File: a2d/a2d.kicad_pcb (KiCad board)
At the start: 4 copper layers, 70 x 65.8 mm, 67 parts, among them CN1 BM04B-SRSS-TB(LF)(SN), U1 B3B-XH-A(LF)(SN), U10 B3B-XH-A(LF)(SN), U2 2060-453/998-404, U3 ADM7150ARDZ-5.0, U4 ADS1115IDGSR, U5 2060-453/998-404, U6 B3B-XH-A(LF)(SN), U7 2060-453/998-404, U8 B3B-XH-A(LF)(SN), U9 2060-453/998-404

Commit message: fix large cap
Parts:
- removed C8: 47uF, Capacitor_SMD:C_0603_1608Metric
- C13: value 47uF -> 47uf; footprint Capacitor_SMD:C_0603_1608Metric -> Capacitor_Tantalum_SMD:CP_EIA-7343-43_Kemet-X
- C18, C2, C22, C26, C27, C7: value .1uf -> 100nf
- moved C13 8.30 mm to (33.3, 30.6), turned to 180 degrees
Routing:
- net +5V: track 35.0 -> 41.3 mm
- net /6V: track 20.4 -> 18.8 mm
- net GND: vias 45 -> 48

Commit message: add second i2c connector
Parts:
- added C14: 1uf, Capacitor_SMD:C_0603_1608Metric, F.Cu at (53.8, 74.0)
- added C29: 10uf, Capacitor_SMD:C_0603_1608Metric, F.Cu at (55.4, 74.0)
- added C8: 100nf, Capacitor_SMD:C_0603_1608Metric, F.Cu at (52.2, 74.0)
- added CN2: BM04B-SRSS-TB(LF)(SN), easyeda2kicad:CONN-SMD_BM04B-SRSS-TB, F.Cu at (50.0, 78.0)
- added D6: SP0503BAHT, Package_TO_SOT_SMD:SOT-143, F.Cu at (49.6, 73.8)
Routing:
- net /6V: track 18.8 -> 101.4 mm, vias 0 -> 5
- net /SCL: track 37.2 -> 66.0 mm, vias 2 -> 3
- net /SDA: track 37.6 -> 63.1 mm, vias 2 -> 3
- net GND: track 63.3 -> 66.8 mm, vias 48 -> 55

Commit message: a2d v0.2
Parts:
- added J1: Conn_02x04_Odd_Even, Connector_PinHeader_2.54mm:PinHeader_2x04_P2.54mm_Vertical, F.Cu at (26.9, 53.8)
- added JP1: Jumper_2_Small_Open, Connector_PinHeader_2.54mm:PinHeader_1x02_P2.54mm_Vertical, F.Cu at (60.8, 49.2)
- added JP2: Jumper_2_Small_Open, Connector_PinHeader_2.54mm:PinHeader_1x02_P2.54mm_Vertical, F.Cu at (61.0, 71.8)
- added JP3: Jumper_2_Small_Open, Connector_PinHeader_2.54mm:PinHeader_1x02_P2.54mm_Vertical, F.Cu at (41.2, 56.6)
- added JP4: Jumper_2_Small_Open, Connector_PinHeader_2.54mm:PinHeader_1x02_P2.54mm_Vertical, F.Cu at (42.8, 32.4)
- C1, C16, C18, C2, C20, C22, C24, C26: value 100nf -> 100nF
- C15, C19, C23, C3: value 10uf -> 10uF
- C17, C21, C25, C4: value 1uf -> 1uF
- R2, R4, R6, R8: value 100k -> 5.1M
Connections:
- R2 pad 1: GND -> Net-(JP1-A)
- R4 pad 1: GND -> Net-(JP2-A)
- R6 pad 1: GND -> Net-(JP3-A)
- R8 pad 1: GND -> Net-(JP4-A)
- U4 pad 1: GND -> Net-(J1-Pin_2)
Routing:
- net Net-(J1-Pin_2): track 0.00 -> 23.2 mm
- net /SCL: track 66.0 -> 86.4 mm, vias 3 -> 5
- net /SDA: track 63.1 -> 79.8 mm
- net Net-(JP1-A): track 0.00 -> 10.5 mm
- net Net-(JP2-A): track 0.00 -> 9.75 mm
- net Net-(JP3-A): track 0.00 -> 9.15 mm
- net Net-(JP4-A): track 0.00 -> 8.03 mm
- net /6V: track 101.4 -> 103.9 mm
- net GND: track 66.8 -> 64.9 mm, vias 55 -> 51
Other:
- board text added: "1"
- board text added: "2"
- board text added: "3"
- board text added: "4"
- board text added: "A2D V0.2"
- board text added: "Address:"
- board text removed: "A2D V0.1"

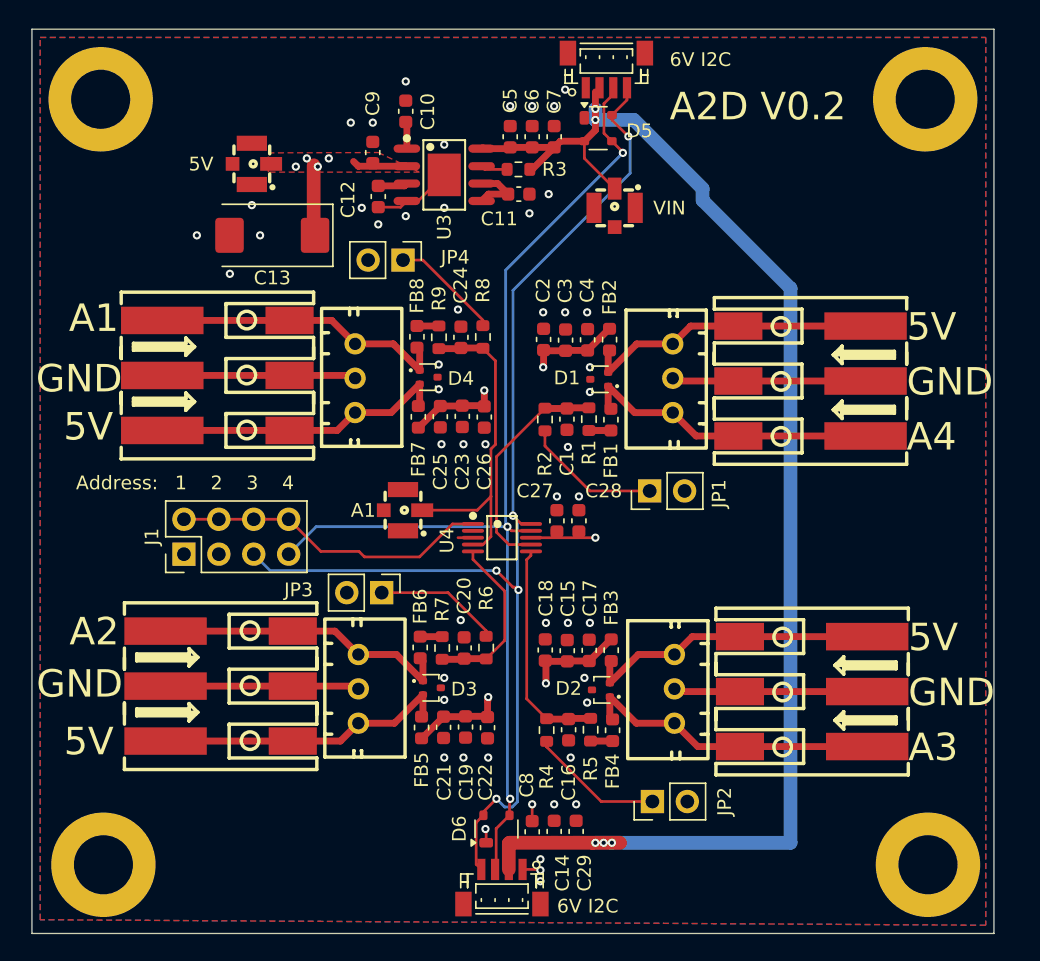
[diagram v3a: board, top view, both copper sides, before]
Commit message: reverse connector orientation for a2d
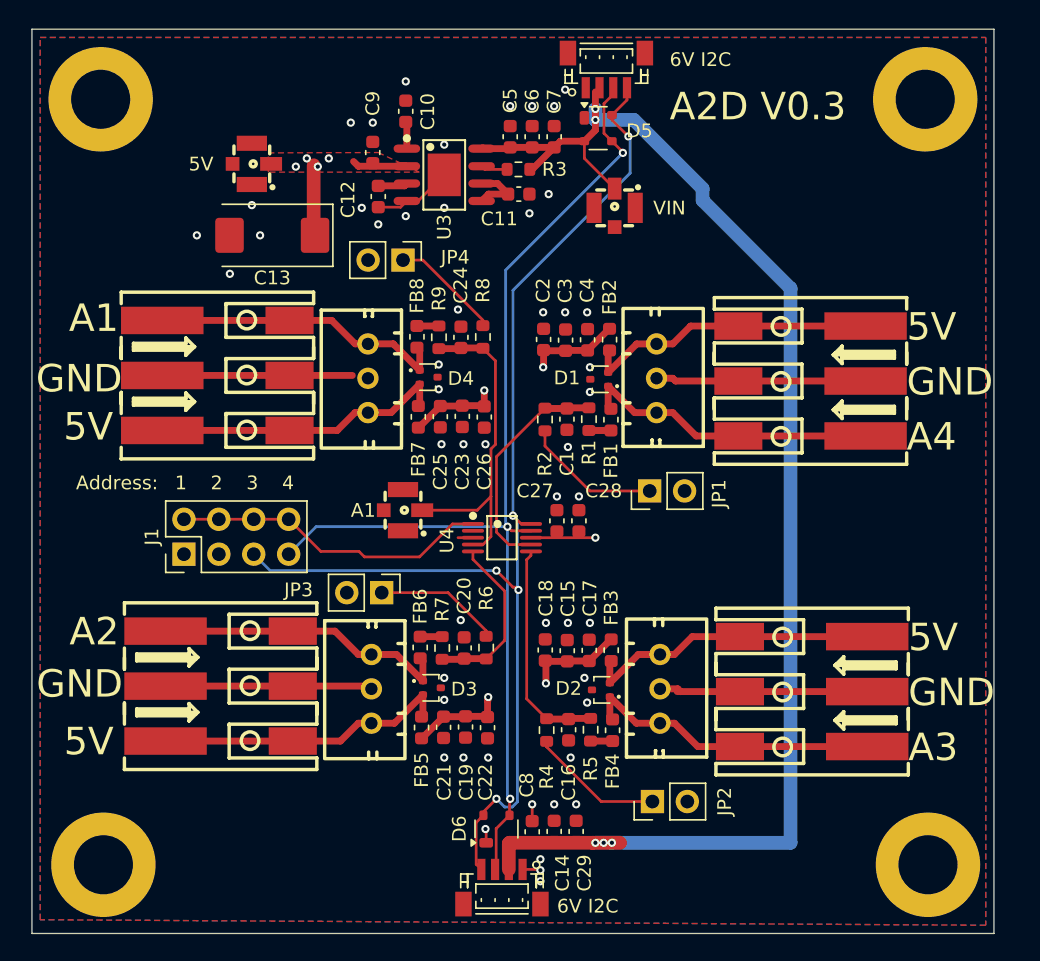
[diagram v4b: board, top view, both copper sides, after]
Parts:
- moved U1 1.18 mm to (61.2, 41.0), turned to 90 degrees
- moved U6 1.05 mm to (61.5, 63.6), turned to 90 degrees
- moved U8 0.95 mm to (40.5, 63.6), turned to -90 degrees
- moved U10 0.94 mm to (40.2, 41.0), turned to -90 degrees
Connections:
- U1 pad 1: Net-(D1-K2) -> Net-(D1-K1)
- U1 pad 3: Net-(D1-K1) -> Net-(D1-K2)
- U10 pad 1: Net-(D4-K2) -> Net-(D4-K1)
- U10 pad 3: Net-(D4-K1) -> Net-(D4-K2)
- U6 pad 1: Net-(D2-K2) -> Net-(D2-K1)
- U6 pad 3: Net-(D2-K1) -> Net-(D2-K2)
- U8 pad 1: Net-(D3-K2) -> Net-(D3-K1)
- U8 pad 3: Net-(D3-K1) -> Net-(D3-K2)
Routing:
- net GND: track 64.9 -> 69.2 mm
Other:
- board text added: "A2D V0.3"
- board text removed: "A2D V0.2"

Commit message: a2d v0.4
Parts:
- removed the C13 at (33.3, 30.6)
- removed the C15 at (54.8, 60.8)
- removed C19: 10uF, Capacitor_SMD:C_0603_1608Metric
- removed C21: 1uF, Capacitor_SMD:C_0603_1608Metric
- removed the C23 at (47.1, 43.8)
- removed the C25 at (45.5, 43.8)
- removed the C3 at (54.6, 38.2)
- removed the C4 at (56.2, 38.2)
- removed JP1, JP2, JP3, JP4: Jumper_2_Small_Open, Connector_PinHeader_2.54mm:PinHeader_1x02_P2.54mm_Vertical
- removed RF3: 73412-0110, easyeda2kicad:ANT-SMD_73412-0110
- removed the U1 at (61.2, 41.0)
- removed U10, U6, U8: B3B-XH-A(LF)(SN), easyeda2kicad:CONN-TH_3P-P2.50_A2501WV2-3P
- removed the U2 at (71.8, 41.2)
- removed U5, U7, U9: 2060-453/998-404, easyeda2kicad:CONN-SMD_2060-453
- added C22: 3.3uF, Capacitor_SMD:C_0603_1608Metric, F.Cu at (52.5, 39.0)
- added C27: 3.3uF, Capacitor_SMD:C_0603_1608Metric, F.Cu at (48.5, 39.0)
- added C32: 3.3uF, Capacitor_SMD:C_0603_1608Metric, F.Cu at (44.5, 37.0)
- added CN3: 39302030, easyeda2kicad:CONN-TH_3P-P4.20_39302030, F.Cu at (78.0, 45.6)
- added CN4: 39302030, easyeda2kicad:CONN-TH_3P-P4.20_39302030, F.Cu at (63.5, 45.6)
- added CN5: 39302030, easyeda2kicad:CONN-TH_3P-P4.20_39302030, F.Cu at (39.0, 45.5)
- added CN6: 39302030, easyeda2kicad:CONN-TH_3P-P4.20_39302030, F.Cu at (24.0, 45.6)
- C17: value 1uF -> 3.3uF
- moved C33 31.4 mm to (17.5, 40.3)
- moved C28 31.1 mm to (32.5, 40.0)
- moved C20 29.2 mm to (52.5, 37.5), turned to 0 degrees
- moved FB5 28.3 mm to (34.0, 40.0), turned to 90 degrees
- moved R4 26.7 mm to (55.7, 40.0), turned to 180 degrees
- moved R5 26.4 mm to (52.5, 40.5), turned to 180 degrees
- moved D6 25.5 mm to (20.5, 49.1), turned to -90 degrees
- moved FB7 25.2 mm to (19.0, 40.3), turned to 90 degrees
- moved C17 23.8 mm to (56.5, 37.0)
- moved FB4 23.3 mm to (55.5, 43.5), turned to 90 degrees
- moved C25 23.2 mm to (48.5, 37.5), turned to 180 degrees
- moved J1 22.6 mm to (20.5, 32.1)
- moved FB2 21.4 mm to (79.0, 40.0), turned to 90 degrees
- moved FB6 21.2 mm to (40.0, 39.8)
- moved R6 21.0 mm to (45.0, 40.0), turned to 0 degrees
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- renumbered C8 to C1, C9 to C10, C28 to C12, C27 to C13, C1 to C15, C2 to C18, C7 to C2, C16 to C20, C18 to C23, C20 to C25, C22 to C28, C14 to C3, C24 to C30, C26 to C33, C6 to C4, C29 to C5, C5 to C6, C11 to C7, C10 to C8, C12 to C9, CN2 to CN1, CN1 to CN2, D6 to D1, D5 to D2, D1 to D3, D2 to D4, D3 to D5, D4 to D6, FB2 to FB1, FB1 to FB2, R3 to R1, R1 to R3, U3 to U1, U4 to U2
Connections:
- C17 pad 1: +5V -> GND
- C17 pad 2: GND -> /A4
- R2 pad 1: Net-(JP1-A) -> GND
- R4 pad 1: Net-(JP2-A) -> GND
- R6 pad 1: Net-(JP3-A) -> GND
- R8 pad 1: Net-(JP4-A) -> GND
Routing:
- net GND: track 69.2 -> 13.8 mm, vias 51 -> 40
- net +5V: track 41.3 -> 21.2 mm
- net Net-(FB2-Pad2): track 1.60 -> 21.6 mm
- net Net-(FB8-Pad2): track 1.60 -> 18.6 mm
- net /A1: track 24.3 -> 7.90 mm
- net Net-(D4-K2): track 21.6 -> 7.34 mm
- net Net-(D6-K2): track 21.6 -> 7.84 mm
- net Net-(D5-K2): track 21.6 -> 8.12 mm
- net Net-(D3-K2): track 21.6 -> 8.75 mm
- net Net-(D5-K1): track 22.0 -> 9.16 mm
- net Net-(D6-K1): track 22.0 -> 9.41 mm
- net Net-(D3-K1): track 22.0 -> 9.41 mm
- net Net-(JP1-A): track 10.5 -> 0.00 mm
- net Net-(JP2-A): track 9.75 -> 0.00 mm
- net /A3: track 16.0 -> 6.43 mm
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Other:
- board size 70 x 65.8 mm -> 70 x 45 mm
- board text added: "A2D V0.4"
- board text removed: "A2D V0.3"
- board text removed: "GND"
